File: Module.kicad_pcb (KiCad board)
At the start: 6 copper layers, 30 x 41.8 mm, 135 parts

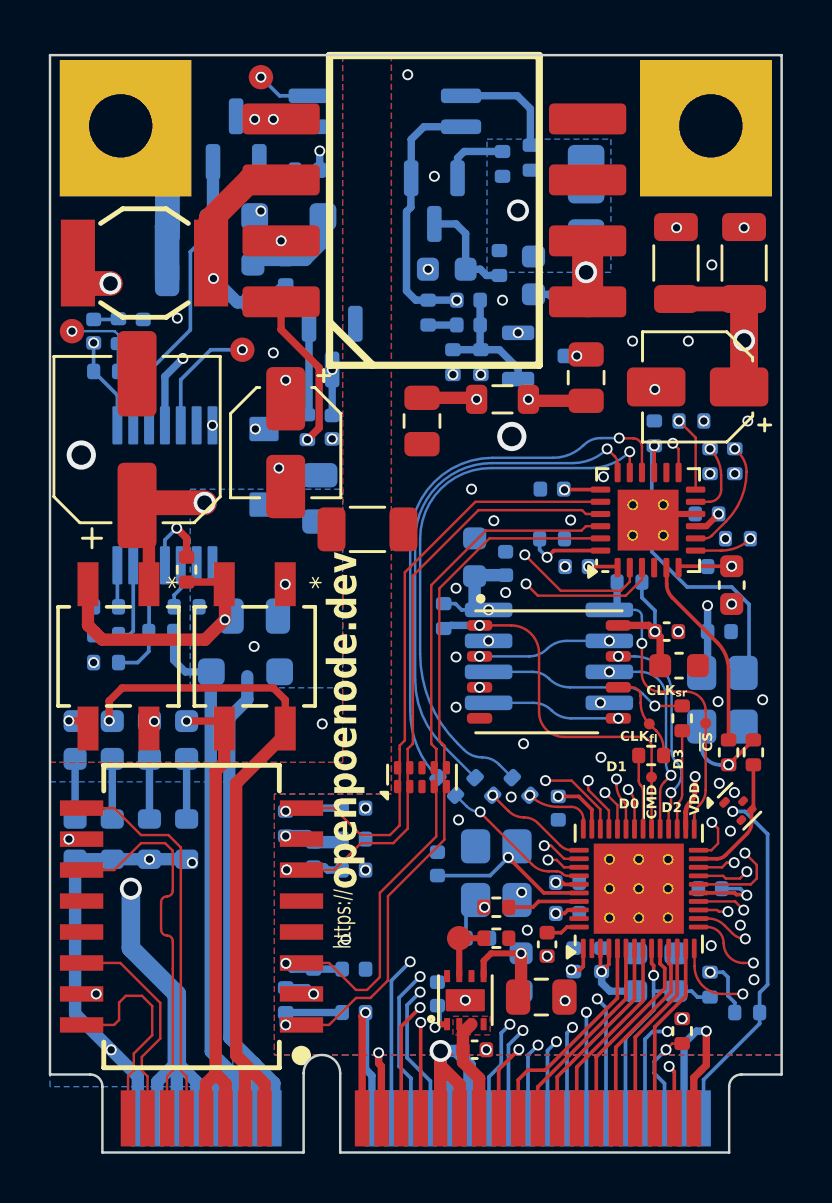
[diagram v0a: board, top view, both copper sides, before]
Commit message: ESP32 silk screen enhancement added missing part numbers finalized r0.3 work optimized Ethernet ESD diode position added second 22uF bulk updated transformer footprint courtyard enlarged supply current testpad tented bottom testpad vias for flash/ram increased bulk capacitance after efuse reverted solder paste reduction repositioning and cleanup, footprint reworks
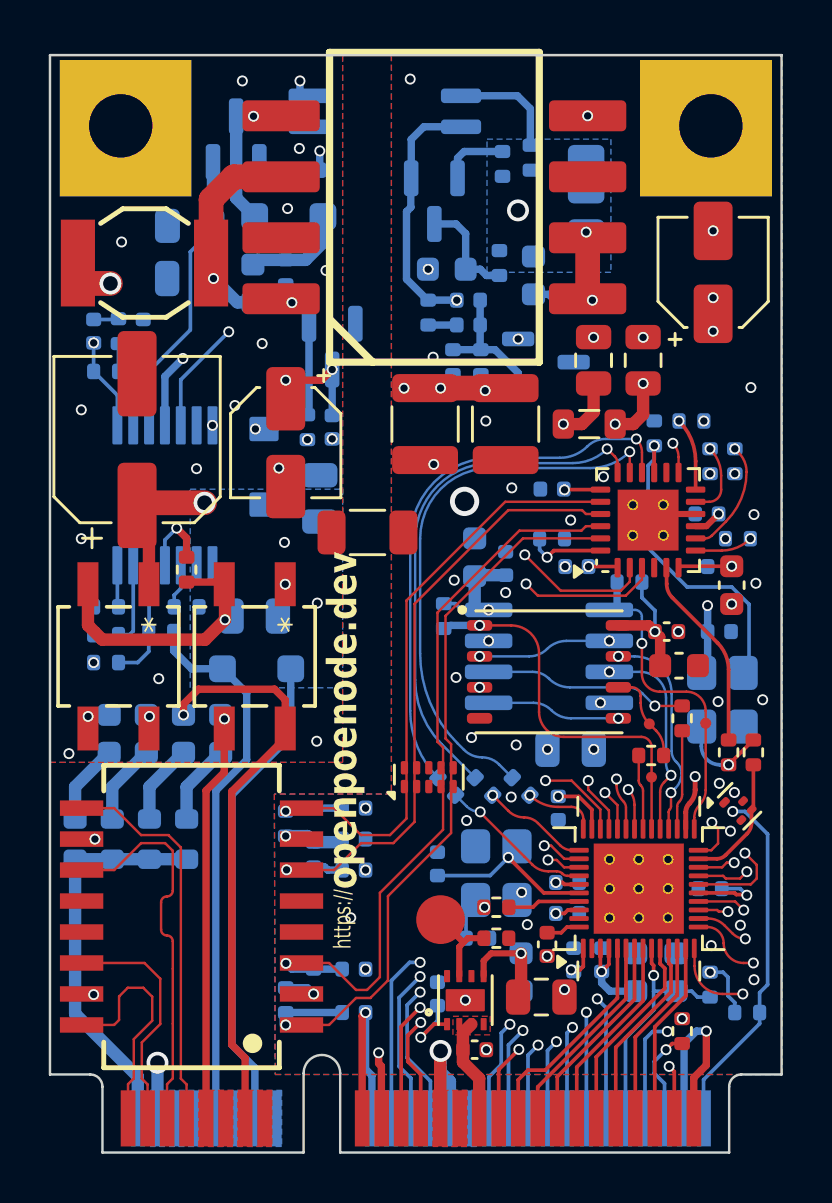
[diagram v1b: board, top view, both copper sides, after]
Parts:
- removed 1TP5, 1TP7, 1TP8: TestPoint, TestPoint:TestPoint_Pad_D1.0mm
- added 2C40: 22uF, Capacitor_SMD:C_0805_2012Metric, B.Cu at (6.35, -13.3)
- 1C1, 1C2: footprint Capacitor_SMD:C_1206_3216Metric -> Capacitor_SMD:C_1210_3225Metric
- 1C13: value 10uF -> 22uF
- 1TP1: footprint TestPoint:TestPoint_Pad_D1.0mm -> TestPoint:TestPoint_Pad_D2.0mm
- moved 1C1 12.2 mm to (0.38, -26.7), turned to -90 degrees
- moved 1C2 11.8 mm to (3.68, -26.7), turned to -90 degrees
- moved 1C5 7.46 mm to (7.29, -29.3), turned to 90 degrees
- moved 1C4 4.74 mm to (12.2, -32.9), turned to 90 degrees
- moved 1L2 3.70 mm to (7.11, -26.7)
- moved 2C21 2.93 mm to (-9.53, -14.0)
- moved 1C3 2.44 mm to (9.32, -29.3)
- moved 2R31 1.52 mm to (-12.4, -9.65)
- moved 2R32 1.52 mm to (-10.9, -9.65)
- moved 2C19 1.42 mm to (-8.00, -14.0)
- moved 2C22 1.42 mm to (-12.6, -14.0)
- moved 1TP1 1.08 mm to (1.02, -6.35)
- moved 2D6 0.47 mm to (-6.53, -16.6)
- moved 2C20 0.28 mm to (-11.0, -14.0)
- moved 1D3 0.28 mm to (0.53, -12.2)
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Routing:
- net /Vout: track 47.8 -> 9.73 mm, vias 4 -> 7
- net GNDPWR: track 41.8 -> 27.3 mm, vias 10 -> 19
- net /P4: track 29.2 -> 23.3 mm
- net /P3: track 20.0 -> 16.3 mm
- net Net-(2D1-A): track 5.40 -> 2.50 mm, vias 1 -> 2
- net Net-(2U2-VB): track 6.96 -> 4.63 mm, vias 1 -> 0
- net Net-(2U2-CTL): track 21.7 -> 19.6 mm
- net /Vin: track 24.2 -> 22.5 mm
- net /Vdd: track 29.8 -> 28.2 mm
- net Net-(1U5-DVDT): track 1.57 -> 2.89 mm
- net Net-(1U5-ILM): track 2.57 -> 3.69 mm
- net +3.3VA: track 54.5 -> 53.7 mm
- net Net-(2C22-Pad2): track 2.46 -> 3.30 mm
- net Net-(2C21-Pad2): track 2.46 -> 3.30 mm
- net Net-(2C20-Pad2): track 2.46 -> 3.30 mm
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- added copper zone on F.Cu, net /P3
- added copper zone on F.Cu, net /P4
- added copper zone on B.Cu, net /Vin
- added copper zone on F.Cu, net /Vout
- removed copper zone on B.Cu, net /BST
- removed copper zone on In1.Cu, net /BST
- removed copper zone on In2.Cu, net /BST
- removed copper zone on In3.Cu, net /BST
- removed copper zone on In4.Cu, net /BST
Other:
- board text removed: "CLK_{fl}"
- board text removed: "CLK_{sr}"
- board text removed: "D0"
- board text removed: "D1"
- board text removed: "D2"
- board text removed: "D3"
- board text removed: "VDD"
- board text removed: "~{CMD}"
- board text removed: "~{CS}"
